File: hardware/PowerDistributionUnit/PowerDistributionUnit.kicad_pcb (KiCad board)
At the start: 2 copper layers, 99.1 x 60.2 mm, 101 parts, among them J1 973582101, J2 973582100, J3 973582101, J4 973582100, Q1 SQJ141ELP, Q2 CSD18511Q5A, SW1 SW_Push, U1 TPS25983, U2 AD5258, U3 NUCLEO_L432KC

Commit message: changed led, maybe some other stuff
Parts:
- removed C11, C16: 4.7n, Capacitor_SMD:C_0805_2012Metric
- removed C14: 47n, Capacitor_SMD:C_0805_2012Metric
- removed C17: 10n, Capacitor_SMD:C_0805_2012Metric
- removed C5, C8: 2.2n, Capacitor_SMD:C_0805_2012Metric
- removed C9: 220p, Capacitor_SMD:C_0805_2012Metric
- removed H1, H2, H3: MountingHole, MountingHole:MountingHole_3.2mm_M3
- removed JP11: 200 us, Connector_PinHeader_2.54mm:PinHeader_1x02_P2.54mm_Vertical
- removed JP12: 2 ms, Connector_PinHeader_2.54mm:PinHeader_1x02_P2.54mm_Vertical
- removed JP13: 20 ms, Connector_PinHeader_2.54mm:PinHeader_1x02_P2.54mm_Vertical
- removed JP14: 1.5 V/ms, Connector_PinHeader_2.54mm:PinHeader_1x02_P2.54mm_Vertical
- removed JP15: 1 V/ms, Connector_PinHeader_2.54mm:PinHeader_1x02_P2.54mm_Vertical
- removed JP16: 0.5 V/ms, Connector_PinHeader_2.54mm:PinHeader_1x02_P2.54mm_Vertical
- removed JP17: Latching, Connector_PinHeader_2.54mm:PinHeader_1x02_P2.54mm_Vertical
- removed JP18: Inf, Connector_PinHeader_2.54mm:PinHeader_1x02_P2.54mm_Vertical
- removed JP6: 16 (9.3 ms), Connector_PinHeader_2.54mm:PinHeader_1x02_P2.54mm_Vertical
- removed JP7: 915 ms, Connector_PinHeader_2.54mm:PinHeader_1x02_P2.54mm_Vertical
- removed JP79: ~2A, Connector_PinHeader_2.54mm:PinHeader_1x02_P2.54mm_Vertical
- removed JP8: 91.7 ms, Connector_PinHeader_2.54mm:PinHeader_1x02_P2.54mm_Vertical
- removed JP80: ~5A, Connector_PinHeader_2.54mm:PinHeader_1x02_P2.54mm_Vertical
- removed JP81: ~12A, Connector_PinHeader_2.54mm:PinHeader_1x02_P2.54mm_Vertical
- removed JP9: 9.3 ms, Connector_PinHeader_2.54mm:PinHeader_1x02_P2.54mm_Vertical
- removed R58: 294, Resistor_SMD:R_0805_2012Metric
- removed R59: 121, Resistor_SMD:R_0805_2012Metric
- removed TP14: GND, Connector_PinHeader_2.54mm:PinHeader_1x01_P2.54mm_Vertical
- added JP3: JP, Jumper:SolderJumper-2_P1.3mm_Open_RoundedPad1.0x1.5mm, B.Cu at (132.1, 107.2)
- C1, C2, G***, R1, R2, R3, U2: moved to F.Cu
- C15, C3, C35, C7, D2, R10, R9, SW1: moved to B.Cu
- C4: value 22n -> 0.1u
- D1: value 587-1016-247F -> SK6085; footprint PowerDistributionUnitLib:587-1016-247F -> PowerDistributionUnitLib:SK6085
- J1, J3: footprint PowerDistributionUnitLib:973582101 -> PowerDistributionUnitLib:5754
- J2, J4: footprint PowerDistributionUnitLib:973582100 -> PowerDistributionUnitLib:5754
- JP1, JP19, JP77: footprint Connector_PinHeader_2.54mm:PinHeader_1x02_P2.54mm_Vertical -> Jumper:SolderJumper-2_P1.3mm_Open_RoundedPad1.0x1.5mm; moved to B.Cu
- JP2: footprint Connector_PinHeader_2.54mm:PinHeader_1x02_P2.54mm_Vertical -> Jumper:SolderJumper-2_P1.3mm_Open_TrianglePad1.0x1.5mm
- JP4: value 16 (915 ms) -> JP; footprint Connector_PinHeader_2.54mm:PinHeader_1x02_P2.54mm_Vertical -> Jumper:SolderJumper-2_P1.3mm_Open_RoundedPad1.0x1.5mm; moved to B.Cu
- JP5: value 16 (91.7 ms) -> JP; footprint Connector_PinHeader_2.54mm:PinHeader_1x02_P2.54mm_Vertical -> Jumper:SolderJumper-2_P1.3mm_Open_RoundedPad1.0x1.5mm; moved to B.Cu
- TP10: value Conn_01x02 -> IN_SENSE; footprint Connector_PinHeader_2.54mm:PinHeader_1x02_P2.54mm_Vertical -> TestPoint:TestPoint_Pad_D1.0mm
- moved TP8 64.1 mm to (155.7, 92.5)
- moved TP10 63.5 mm to (160.3, 115.8), turned to 0 degrees
- moved G*** 61.3 mm to (125.0, 111.3), turned to 0 degrees
- moved D1 60.3 mm to (155.4, 119.3)
- moved TP4 56.9 mm to (164.1, 112.0)
- moved R9 50.8 mm to (127.0, 116.2)
- moved TP6 47.8 mm to (132.8, 94.2)
- moved C10 46.9 mm to (133.2, 90.9), turned to 90 degrees
- moved TP3 43.6 mm to (135.4, 85.9)
- moved SW1 42.1 mm to (120.9, 114.8)
- moved C7 42.0 mm to (139.0, 90.9), turned to 90 degrees
- moved TP5 41.9 mm to (160.3, 112.0)
- moved TP76 40.1 mm to (125.7, 74.4)
- moved C15 38.4 mm to (141.7, 87.0), turned to 90 degrees
- moved TP1 36.4 mm to (141.7, 84.1)
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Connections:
- C10 pad 1: Net-(JP11-A) -> GND
- C15 pad 1: Net-(JP14-A) -> GND
- C3 pad 1: Net-(JP4-A) -> GND
- C4 pad 1: Net-(JP5-A) -> +3V3
- C4 pad 2: /NRETRY -> GND
- C7 pad 1: Net-(JP7-A) -> GND
- D1 pad 1: GND -> /LED_D
- D1 pad 2: unconnected-(D1-SDO-Pad2) -> +3V3
- D1 pad 4: +3V3 -> GND
- JP1 pad 2: /ILIM -> /ILIM_SDA
- JP4 pad 2: GND -> /ILIM_SCL
- JP5 pad 2: GND -> /ILIM_SDA
- R57 pad 1: Net-(JP79-A) -> GND
- R8 pad 2: GND -> GNDPWR
- TP10 pad 1: /LED_CK -> /LED_D
- U2 pad 1: Net-(JP1-A) -> /ILIM
- U3 pad CN3_12: /IND_BTN -> unconnected-(U3-PA8-PadCN3_12)
- U3 pad CN3_5: unconnected-(U3-PA12-PadCN3_5) -> /IND_BTN
- U3 pad CN3_7: unconnected-(U3-PB7-PadCN3_7) -> Net-(JP5-A)
- U3 pad CN3_8: unconnected-(U3-PB6-PadCN3_8) -> Net-(JP4-A)
- U3 pad CN4_10: Net-(JP19-A) -> /PG
- U3 pad CN4_11: /LED_CK -> unconnected-(U3-PA1-PadCN4_11)
- U3 pad CN4_12: /LED_SD -> /LED_D
- U3 pad CN4_5: /PG -> Net-(JP19-A)
- U3 pad CN4_7: /ILIM_SCL -> Net-(JP3-A)
- U3 pad CN4_8: /ILIM_SDA -> Net-(JP1-A)
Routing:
- net /dVdt/BGATE: track 50.7 -> 5.78 mm, vias 2 -> 1
- net /NRETRY: track 47.8 -> 7.70 mm, vias 2 -> 1
- net /LED_CK: track 40.1 -> 0.00 mm
- net /ITIMER: track 45.6 -> 7.50 mm, vias 2 -> 1
- net /RETRY_DLY: track 44.8 -> 7.03 mm, vias 2 -> 1
- net /LED_SD: track 37.7 -> 0.00 mm
- net /IND_BTN: track 46.7 -> 12.7 mm
- net /ILIM: track 35.9 -> 9.11 mm, vias 2 -> 1
- net /LED_D: track 0.00 -> 25.3 mm
- net /IN: track 6.32 -> 28.6 mm, vias 0 -> 1
- net /IN_SENSE: track 45.7 -> 61.6 mm
- net GND: track 14.0 -> 0.00 mm, vias 52 -> 3
- net /IMON: track 35.9 -> 24.6 mm
- net /PG: track 41.4 -> 30.5 mm
- net GNDPWR: track 2.25 -> 12.1 mm
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- removed copper zone on B.Cu, net /EFUSE_IN
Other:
- board size 99.1 x 60.2 mm -> 54.9 x 50 mm
- board text added: "3.3V"
- board text added: "EFET Out"
- board text added: "EN"
- board text added: "EN PIN"
- board text added: "GNDPWR"
- board text added: "IN_sens"
- board text added: "ITMR IMON NRTY ILIM RTYDLY UVLO"
- board text added: "LED_D"
- board text added: "OVLO EN"
- board text added: "RPP Bypass"
- board text added: "Watts Yasueda"
- board text added: "dvdt"
- board text added: "eFuse Out"
- board text removed: "(A)"
- board text removed: "(V/ms)"
- board text removed: "(ms)"
- board text removed: "(ns)"
- board text removed: "+3V3"
- board text removed: "0.2"
- board text removed: "0.5"
- board text removed: "1"
- board text removed: "1.5"
- board text removed: "12"
- board text removed: "16"
- board text removed: "2"
- board text removed: "20"
- board text removed: "5"
- board text removed: "9.3"
- board text removed: "91.7"
- board text removed: "915"
- board text removed: "C9"
- board text removed: "CK"
- board text removed: "EFET_S"
- board text removed: "EFUSE_OUT"
- board text removed: "Fuse"
- board text removed: "ILIM"
- board text removed: "ILIM MUST NOT BE OPEN!!!"
- board text removed: "IMON"
- board text removed: "IN_SENSE"
- board text removed: "ITIMER"
- board text removed: "LED"
- board text removed: "NRETRY"
- board text removed: "NUCLEO: L432KC"
- board text removed: "OVLO"
- board text removed: "OVLO Enable"
- board text removed: "PRG"
- board text removed: "RETRY_DLY"
- board text removed: "Rev Pol Bypass"
- board text removed: "Reverse Polarity Protection"
- board text removed: "SD"
- board text removed: "SLEW RATE"
- board text removed: "Wataru Yasueda"
- board text removed: "dvdt/ BGATE"
- board text removed: "eFuse"
- board text removed: "eFuse EN Control Enable"
- board text removed: "∞"

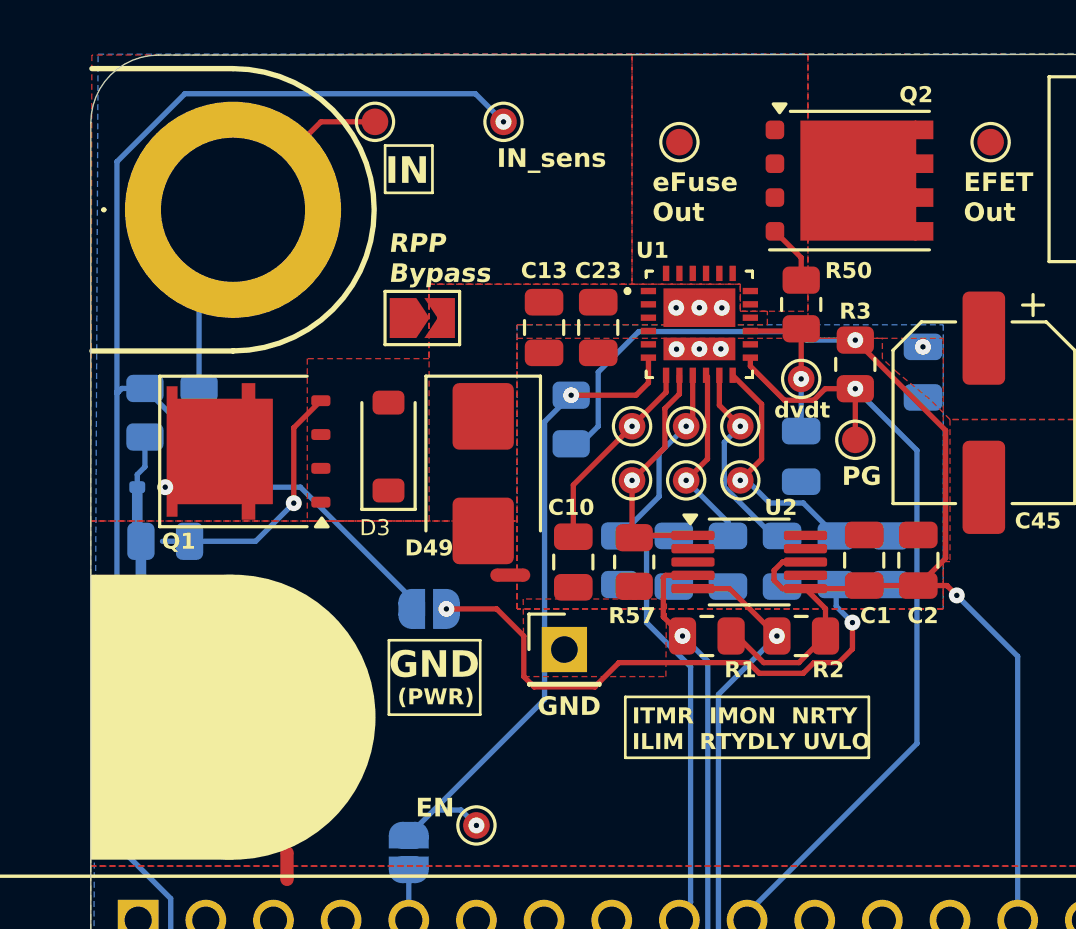
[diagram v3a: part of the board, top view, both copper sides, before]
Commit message: Resolved DRC errors
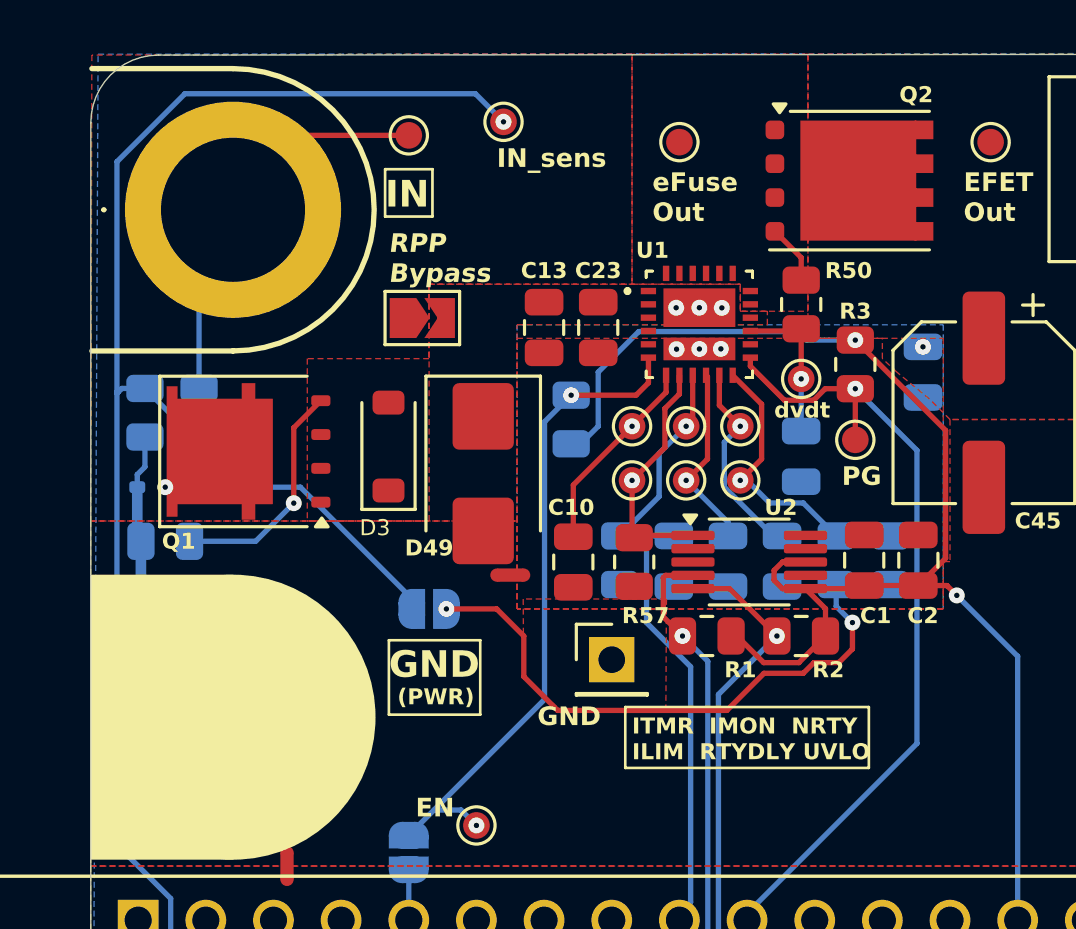
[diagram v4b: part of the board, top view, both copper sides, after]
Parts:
- moved TP6 1.82 mm to (134.6, 94.6)
- moved TP76 1.37 mm to (127.0, 74.9)
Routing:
- net /IN: track 28.6 -> 29.6 mm
- net Net-(D3-A): track 9.79 -> 8.77 mm

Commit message: branched some stuff
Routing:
- net GND: track 0.00 -> 3.44 mm
- net Net-(D3-A): track 8.77 -> 11.3 mm

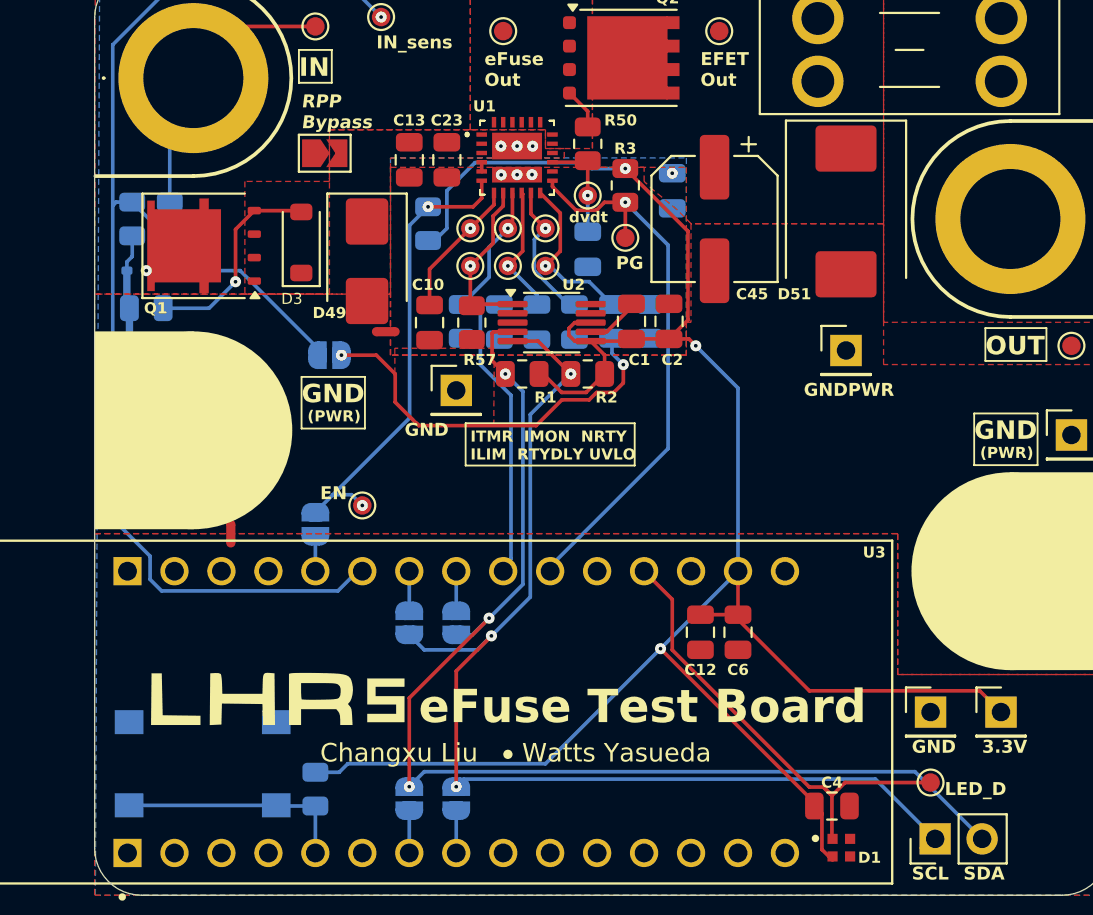
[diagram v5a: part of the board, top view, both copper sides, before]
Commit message: fixed some connections and drc errors
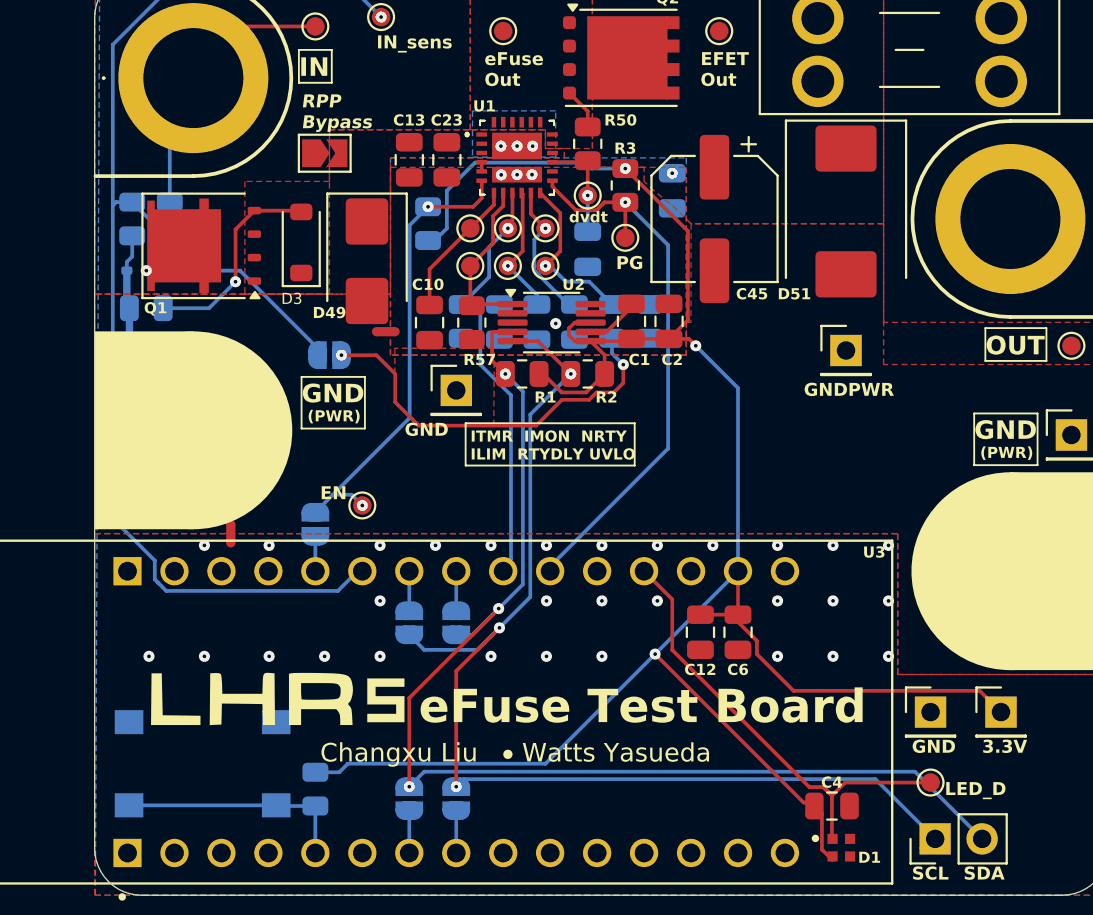
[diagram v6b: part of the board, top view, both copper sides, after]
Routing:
- net /ILIM_SDA: track 63.9 -> 64.6 mm
- net +3V3: track 116.8 -> 117.4 mm
- net /ILIM_SCL: track 61.8 -> 62.4 mm
- net GND: vias 3 -> 34
- net /ITIMER: vias 1 -> 0
- net /ILIM: vias 1 -> 0
- added copper zone on B.Cu, net /EFUSE_IN
